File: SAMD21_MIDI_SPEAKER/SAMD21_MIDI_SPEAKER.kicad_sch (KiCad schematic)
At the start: 11 parts, among them J1 USB_A, J2 54-00175, J3 Screw_Terminal_01x02, J4 Screw_Terminal_01x02, U1 Teensy4.0, U2 AK4432VT, U3 PAM8019KGR

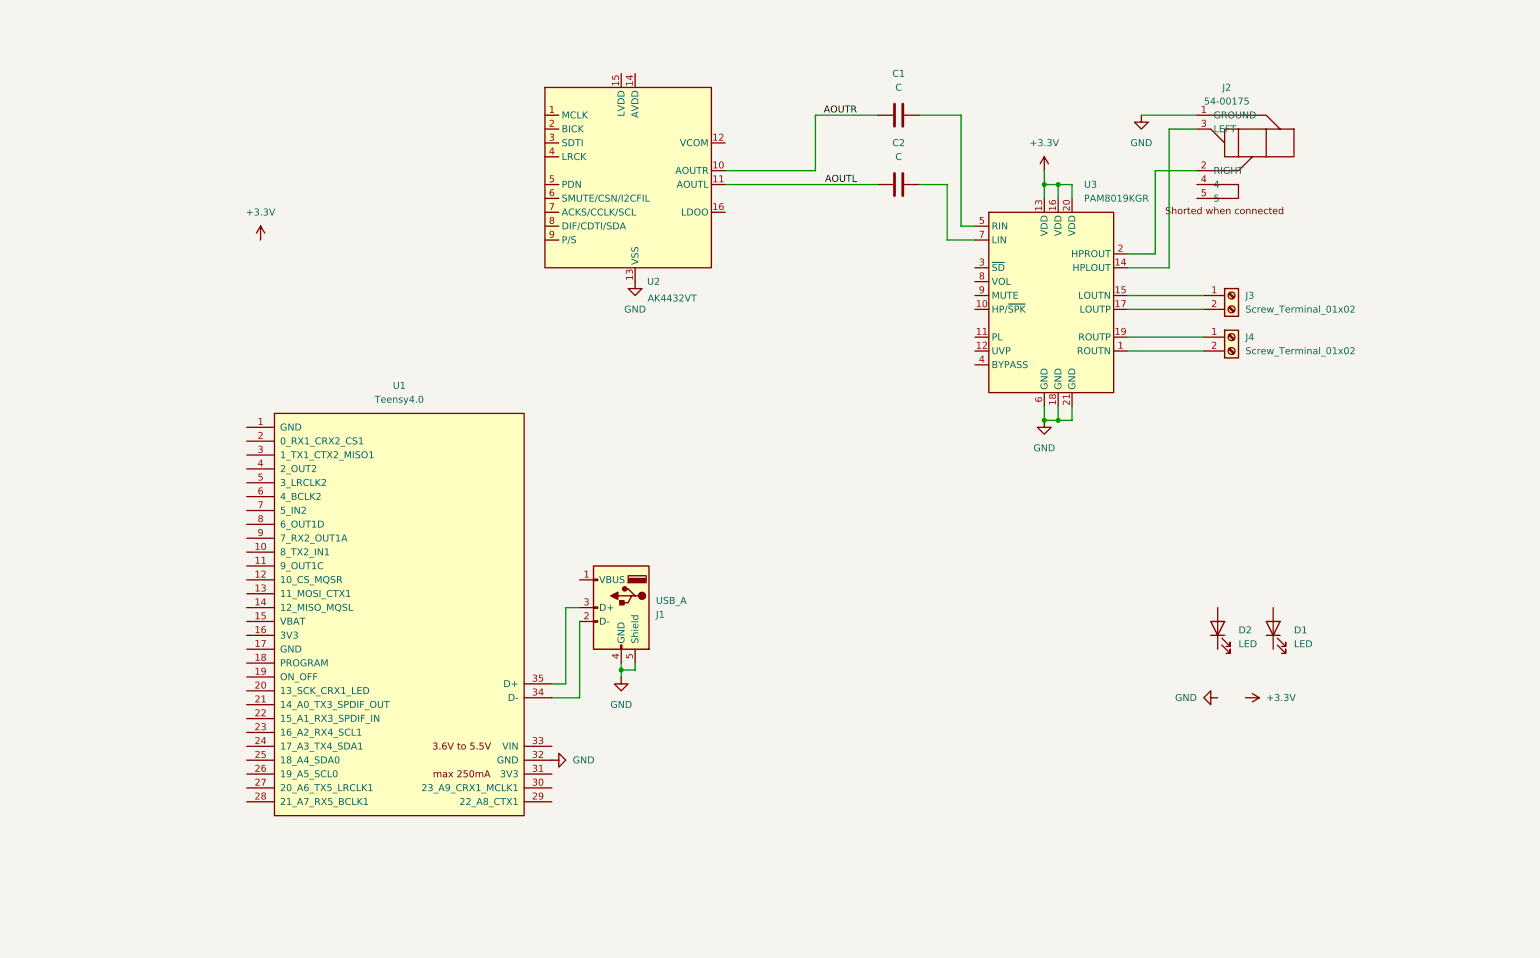
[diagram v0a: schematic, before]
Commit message: Updated schematic to include audio codec, battery charging circuit
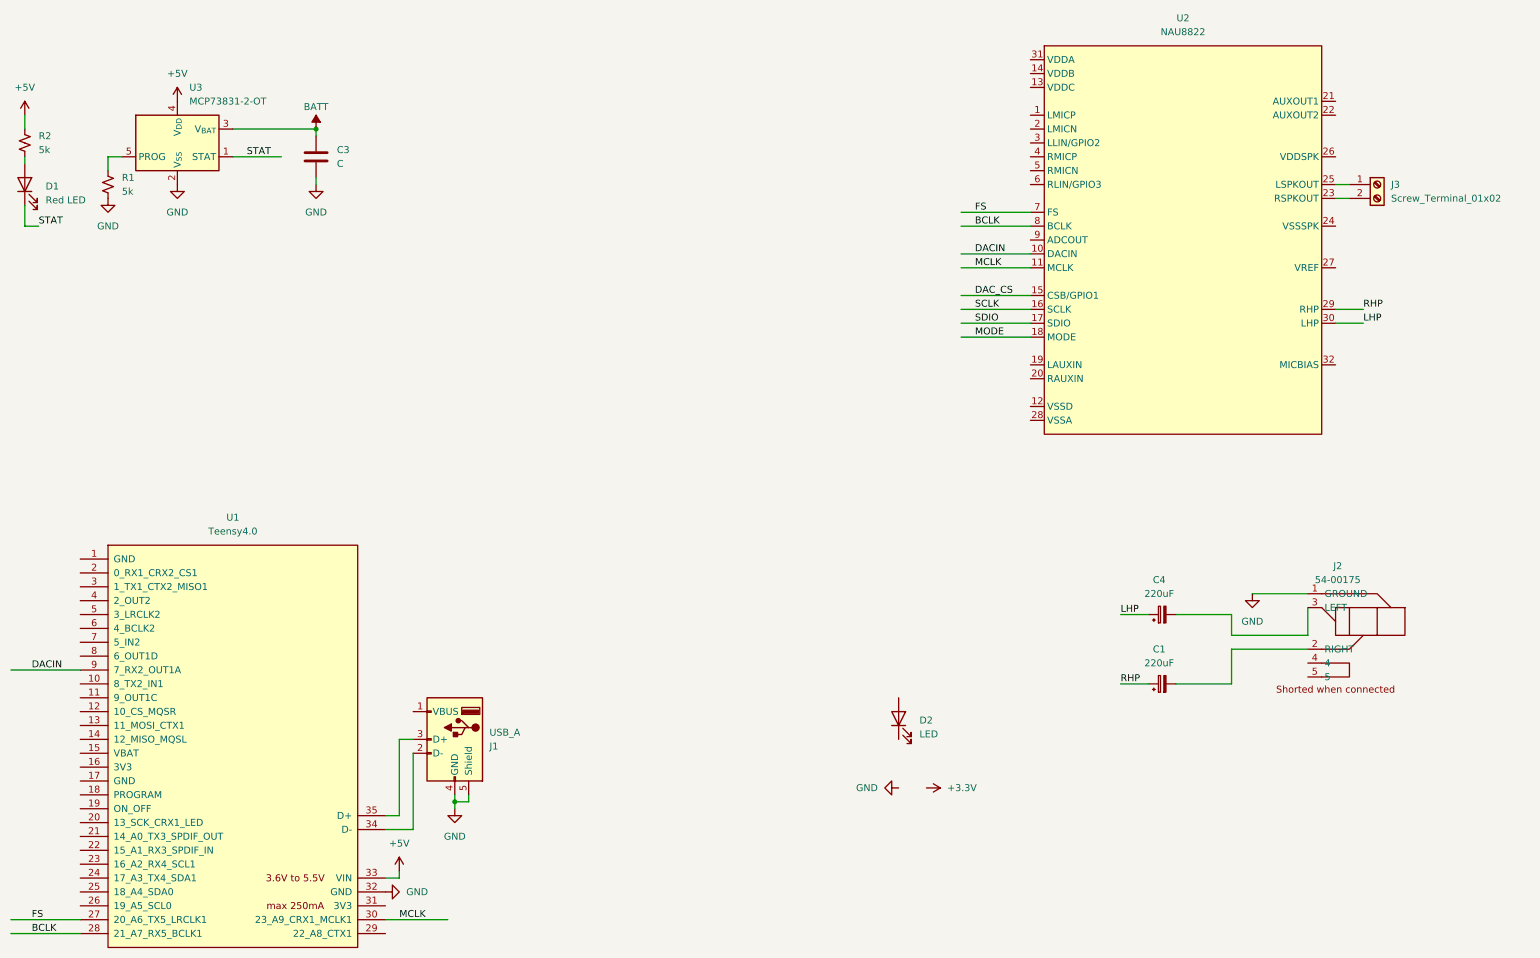
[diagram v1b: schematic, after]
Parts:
- removed C1, C2: C, Capacitor_SMD:C_0603_1608Metric, symbol Device:C
- removed J4: Screw_Terminal_01x02, symbol Connector:Screw_Terminal_01x02
- removed U2: AK4432VT, Package_SO:TSSOP-16_4.4x5mm_P0.65mm, symbol tim:AK4432VT
- removed U3: PAM8019KGR, Package_DFN_QFN:QFN-20-1EP_4x4mm_P0.5mm_EP2.5x2.5mm, symbol tim:PAM8019
- added C1, C4: 220uF, symbol Device:C_Polarized_Small
- added C3: C, Capacitor_SMD:C_0603_1608Metric, symbol Device:C
- added R1, R2: 5k, Resistor_SMD:R_0603_1608Metric, symbol Device:R_Small_US
- added U2: NAU8822, Package_DFN_QFN:QFN-32-1EP_5x5mm_P0.5mm_EP3.1x3.1mm, symbol tim:NAU8822
- added U3: MCP73831-2-OT, Package_TO_SOT_SMD:SOT-23-5, symbol Battery_Management:MCP73831-2-OT
- D1: value LED -> Red LED
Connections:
- net GND: now also C3.1, R1.2, U3.2 (V_{SS})
- net at J2.3 (LEFT): now also C4.2
- net at J3.1 (Pin_1): now also U2.25 (LSPKOUT)
- net at J3.2 (Pin_2): now also U2.23 (RSPKOUT)
- net at J2.2 (RIGHT): now also C1.2
- net STAT: now reaches D1.1 (K)
- net STAT: now also U3.1 (STAT)
- net at D1.2 (A): now also R2.2
- net FS: now reaches U1.27 (20_A6_TX5_LRCLK1)
- net FS: now also U2.7 (FS)
- net BCLK: now reaches U1.28 (21_A7_RX5_BCLK1)
- net BCLK: now also U2.8 (BCLK)
- net MCLK: now reaches U1.30 (23_A9_CRX1_MCLK1)
- net MCLK: now also U2.11 (MCLK)
- net +5V: now reaches U1.33 (VIN)
- net +5V: now also R2.1, U3.4 (V_{DD})
- net DACIN: now reaches U1.9 (7_RX2_OUT1A)
- net DACIN: now also U2.10 (DACIN)
- new net: R1.1, U3.5 (PROG)
- new net BATT: C3.2, U3.3 (V_{BAT})
- new net DAC_CS: U2.15 (CSB/GPIO1)
- new net LHP: C4.1, U2.30 (LHP)
- new net MODE: U2.18 (MODE)
- new net RHP: C1.1, U2.29 (RHP)
- new net SCLK: U2.16 (SCLK)
- new net SDIO: U2.17 (SDIO)
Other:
- moved on the sheet: D2, J1, J2, J3, U1
